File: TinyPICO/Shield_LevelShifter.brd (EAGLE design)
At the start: 31.9 x 17.8 mm, 15 parts, among them U4 SN74HCT245DBRDB20-M

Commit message: Fixing some ERC/DRC errors
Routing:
- net B3: track 10.9 -> 14.4 mm
- net B1: track 17.2 -> 19.2 mm
- net B2: track 14.3 -> 16.3 mm
- net B8: track 4.97 -> 6.37 mm
- net B6: track 5.07 -> 6.18 mm
- net GND: track 42.6 -> 43.4 mm
- net B4: track 9.90 -> 10.6 mm
- net B7: track 6.46 -> 7.17 mm
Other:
- board text added: "LEVEL SHIFTER v2.0"
- board text removed: "LEVEL SHIFTER v1"

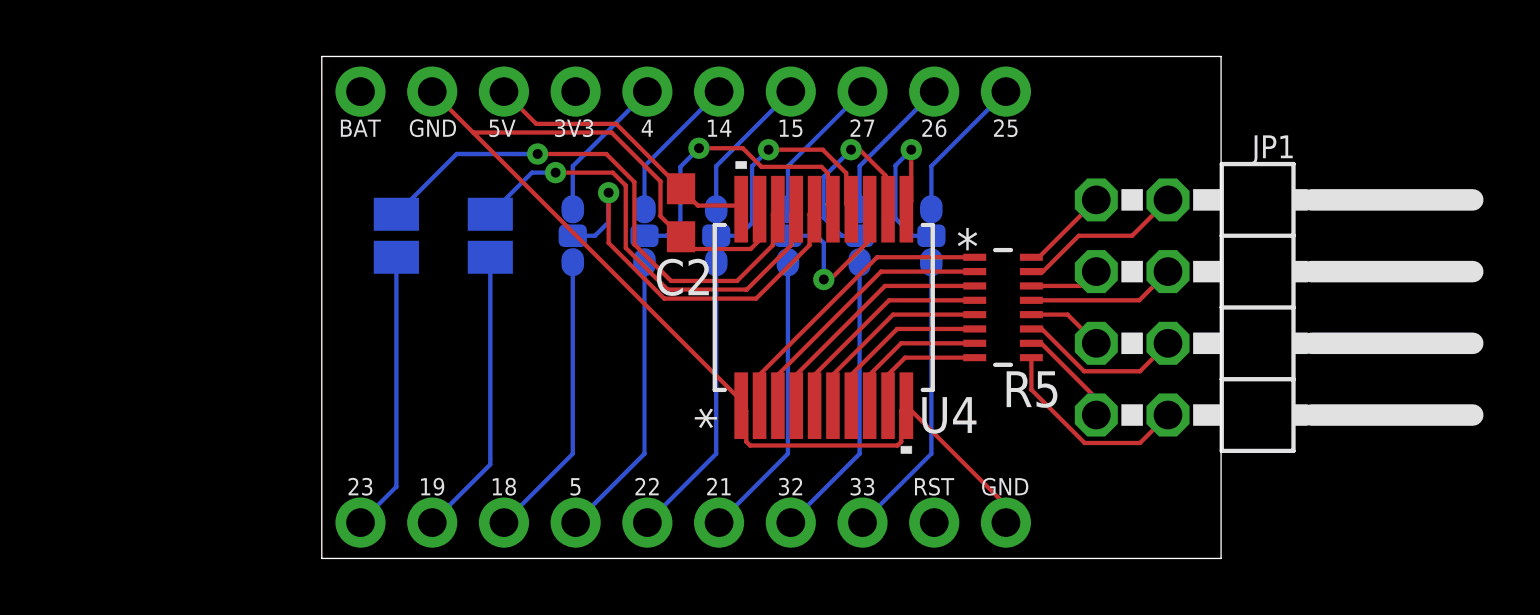
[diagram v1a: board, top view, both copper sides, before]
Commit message: Rotated the board per Seon's suggestion
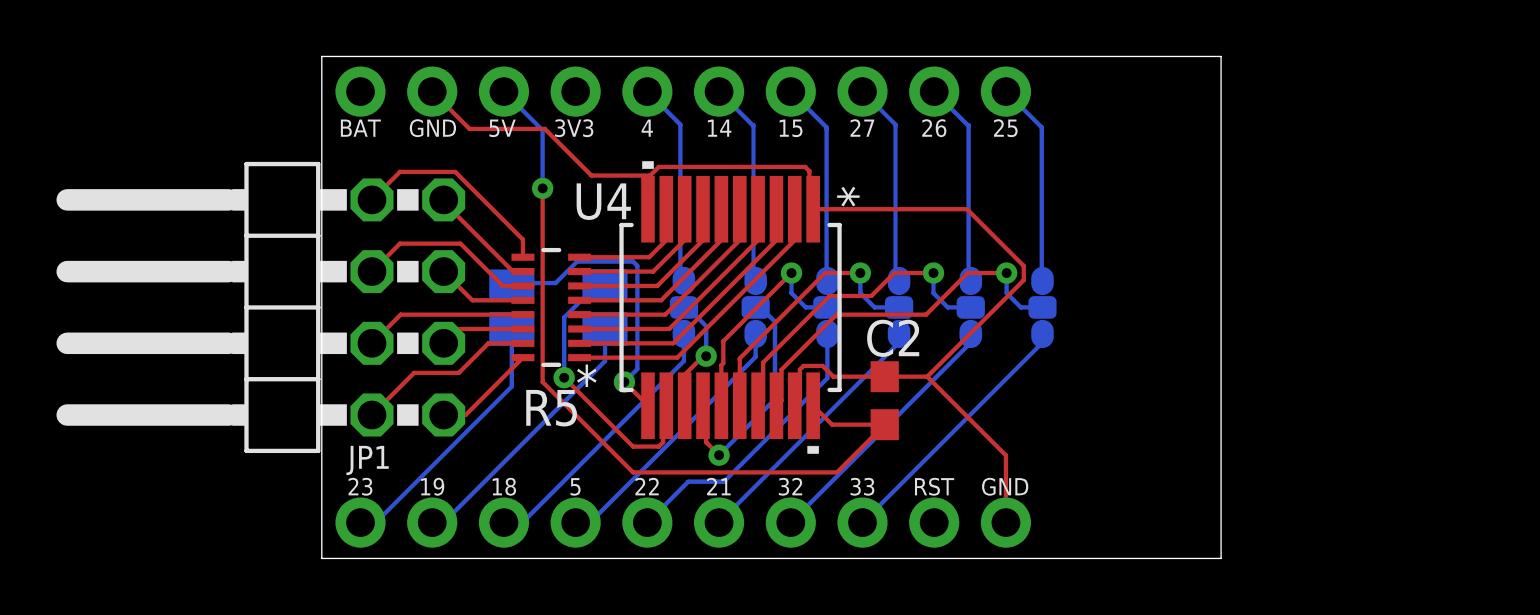
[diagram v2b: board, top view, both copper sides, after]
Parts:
- removed LOGO1: OSHW-LOGOS, SparkFun-Aesthetics:OSHW-LOGO-S
- added LOGO: OSHW-LOGOS, SparkFun-Aesthetics:OSHW-LOGO-S
- 1, 2: value (none) -> 0R-JUMPD; device jumper:SJ -> pv_jump-0r-smd:C0R-JMP_NONE
- 7, 8: value 0R-JUMPD -> (none); device pv_jump-0r-smd:C0R-JMP_NONE -> jumper:SJ
- C2: value (none) -> 0.1uF
- moved JP1 35.8 mm to (-2.03, 8.89), turned to 90 degrees
- moved 1 23.0 mm to (25.5, 8.89), turned to 180 degrees
- moved 2 17.2 mm to (23.0, 8.89), turned to 180 degrees
- moved R5 16.0 mm to (8.13, 8.89), turned to 180 degrees
- moved 8 15.1 mm to (6.73, 8.89), turned to 270 degrees
- moved 3 11.8 mm to (20.4, 8.89)
- moved C2 9.81 mm to (19.9, 5.59), turned to 90 degrees
- moved 7 9.37 mm to (10.0, 8.89), turned to 270 degrees
- moved 4 6.96 mm to (17.9, 8.89)
- moved 6 4.47 mm to (12.8, 8.89)
- moved U4 3.30 mm to (14.5, 8.89), turned to 270 degrees
- moved 5 2.90 mm to (15.4, 8.89)
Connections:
- net B1: now also 1.2; no longer 1.1
- net B2: now also 2.2; no longer 2.1
- net B7: now also 7.1; no longer 7.2
- net B8: now also 8.1; no longer 8.2
- net GPIO14: now also 5.3; no longer 4.3
- net GPIO15: now also 4.3; no longer 5.3
- net GPIO18: now also 6.1; no longer 3.1
- net GPIO19: now also 7.2; no longer 2.2
- net GPIO21: now also 3.1; no longer 6.1
- net GPIO22: now also 4.1; no longer 5.1
- net GPIO23: now also 8.2; no longer 1.2
- net GPIO25: now also 1.3; no longer 8.3
- net GPIO26: now also 2.3; no longer 7.3
- net GPIO27: now also 3.3; no longer 6.3
- net GPIO32: now also 2.1; no longer 7.1
- net GPIO33: now also 1.1; no longer 8.1
- net GPIO4: now also 6.3; no longer 3.3
- net GPIO5: now also 5.1; no longer 4.1
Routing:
- net 5V: track 10.2 -> 27.8 mm, vias 0 -> 1
- net B1: track 19.2 -> 12.9 mm
- net B2: track 16.3 -> 11.2 mm
- net B3: track 14.4 -> 9.49 mm
- net B8: track 6.37 -> 10.4 mm
- net B7: track 7.17 -> 9.97 mm
- net B4: track 10.6 -> 7.92 mm
- net GPIO27: track 5.26 -> 7.26 mm
- net GPIO4: track 5.26 -> 7.26 mm
- net GPIO14: track 5.26 -> 7.26 mm
- net GPIO26: track 5.26 -> 7.26 mm
- net GPIO15: track 5.26 -> 7.24 mm
- net GPIO25: track 5.26 -> 7.24 mm
- net B6: track 6.18 -> 4.27 mm
- net GPIO32: track 10.2 -> 9.32 mm
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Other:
- board text added: "LEVEL SHIFTER 2.0"
- board text removed: "LEVEL SHIFTER v2.0"
